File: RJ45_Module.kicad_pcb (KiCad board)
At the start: 4 copper layers, 36 x 16 mm, 5 parts, among them J1 RJHSE3380A1, J2 Conn_01x13_MountingPin

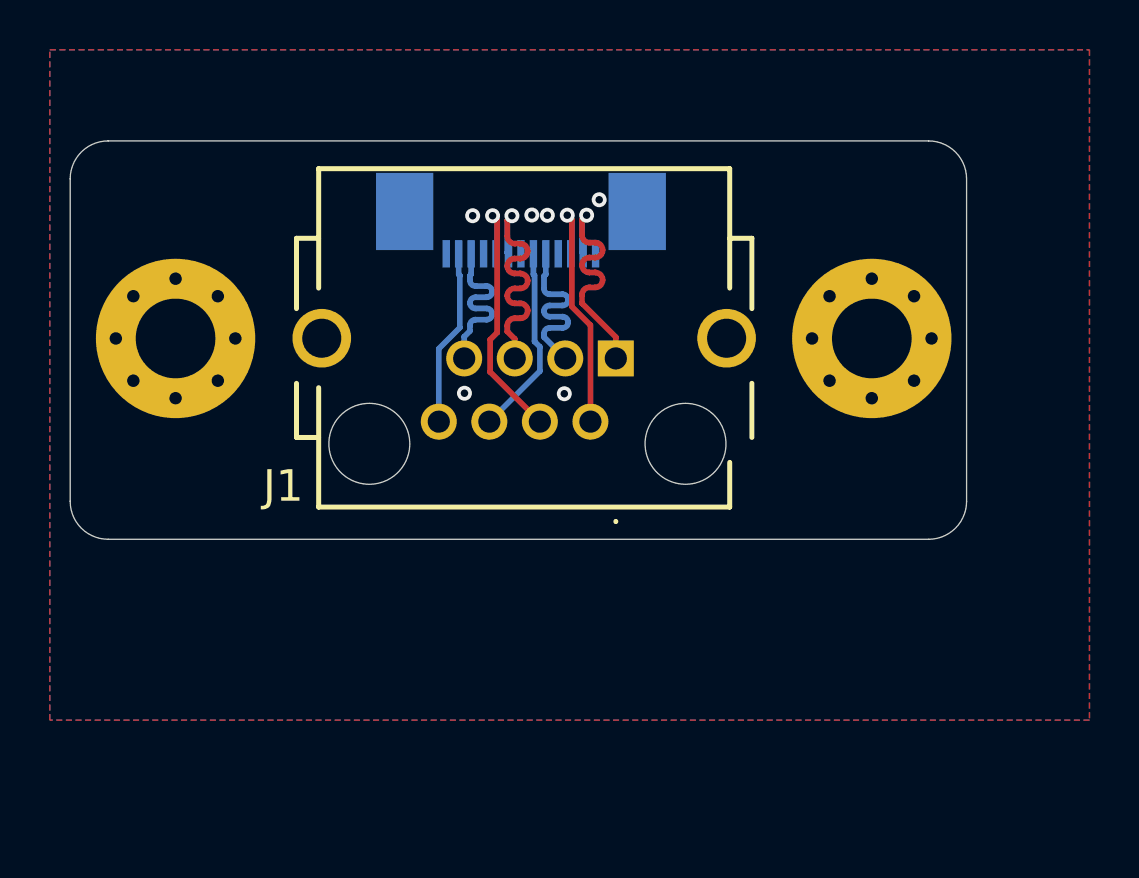
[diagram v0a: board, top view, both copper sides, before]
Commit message: Mouser bites to mounting holes added
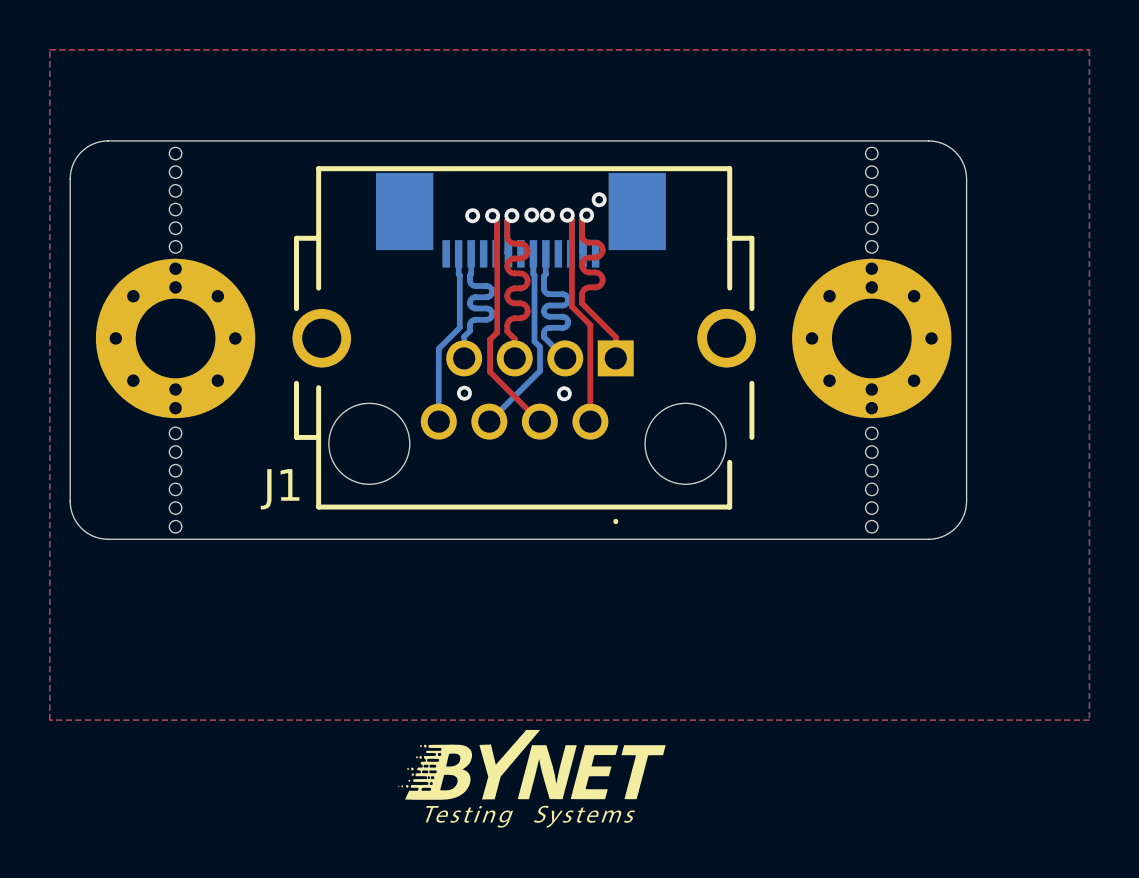
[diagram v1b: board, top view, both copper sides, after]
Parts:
- added  : LOGO, bynet_Logos:BYNET_LOGO_4000x4000, F.Cu at (209.0, 101.4)
- added ?: , clipboard:084e3701-6fdb-4a18-b54f-a9b4173997b9, F.Cu at (222.9, 77.1)
- added ?: , clipboard:084e3701-6fdb-4a18-b54f-a9b4173997b9, F.Cu at (194.9, 77.8)
- added ?: , clipboard:084e3701-6fdb-4a18-b54f-a9b4173997b9, F.Cu at (194.9, 78.6)
- added ?: , clipboard:084e3701-6fdb-4a18-b54f-a9b4173997b9, F.Cu at (194.9, 89.0)
- added ?: , clipboard:084e3701-6fdb-4a18-b54f-a9b4173997b9, F.Cu at (222.9, 80.1)
- added ?: , clipboard:084e3701-6fdb-4a18-b54f-a9b4173997b9, F.Cu at (222.9, 88.3)
- added ?: , clipboard:084e3701-6fdb-4a18-b54f-a9b4173997b9, F.Cu at (194.9, 87.5)
- added ?: , clipboard:084e3701-6fdb-4a18-b54f-a9b4173997b9, F.Cu at (222.9, 78.6)
- added ?: , clipboard:084e3701-6fdb-4a18-b54f-a9b4173997b9, F.Cu at (194.9, 88.3)
- added ?: , clipboard:084e3701-6fdb-4a18-b54f-a9b4173997b9, F.Cu at (222.9, 77.8)
- added ?: , clipboard:084e3701-6fdb-4a18-b54f-a9b4173997b9, F.Cu at (222.9, 91.3)
- added ?: , clipboard:084e3701-6fdb-4a18-b54f-a9b4173997b9, F.Cu at (194.9, 91.3)
- added ?: , clipboard:084e3701-6fdb-4a18-b54f-a9b4173997b9, F.Cu at (194.9, 77.1)
- added ?: , clipboard:084e3701-6fdb-4a18-b54f-a9b4173997b9, F.Cu at (194.9, 89.8)
- added ?: , clipboard:084e3701-6fdb-4a18-b54f-a9b4173997b9, F.Cu at (222.9, 87.5)
- added ?: , clipboard:084e3701-6fdb-4a18-b54f-a9b4173997b9, F.Cu at (222.9, 79.3)
- added ?: , clipboard:084e3701-6fdb-4a18-b54f-a9b4173997b9, F.Cu at (222.9, 90.5)
- added ?: , clipboard:084e3701-6fdb-4a18-b54f-a9b4173997b9, F.Cu at (194.9, 80.1)
- added ?: , clipboard:084e3701-6fdb-4a18-b54f-a9b4173997b9, F.Cu at (194.9, 76.3)
- added ?: , clipboard:084e3701-6fdb-4a18-b54f-a9b4173997b9, F.Cu at (222.9, 89.0)
- added ?: , clipboard:084e3701-6fdb-4a18-b54f-a9b4173997b9, F.Cu at (194.9, 79.3)
- added ?: , clipboard:084e3701-6fdb-4a18-b54f-a9b4173997b9, F.Cu at (222.9, 89.8)
- added ?: , clipboard:084e3701-6fdb-4a18-b54f-a9b4173997b9, F.Cu at (222.9, 76.3)
- added ?: , clipboard:084e3701-6fdb-4a18-b54f-a9b4173997b9, F.Cu at (194.9, 90.5)
